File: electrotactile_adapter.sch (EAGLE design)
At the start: 15 parts, among them J3 PAD_SMD_L0.5_W1, J4 PAD_SMD_L0.5_W1, J5 PAD_SMD_L0.5_W1, J6 PAD_SMD_L0.5_W1, J7 1X33_MOLEX_FPC_FPC_RIBBON-CAB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, J8 1X33_MOLEX_FPC_FPC_RIBBON-CAB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

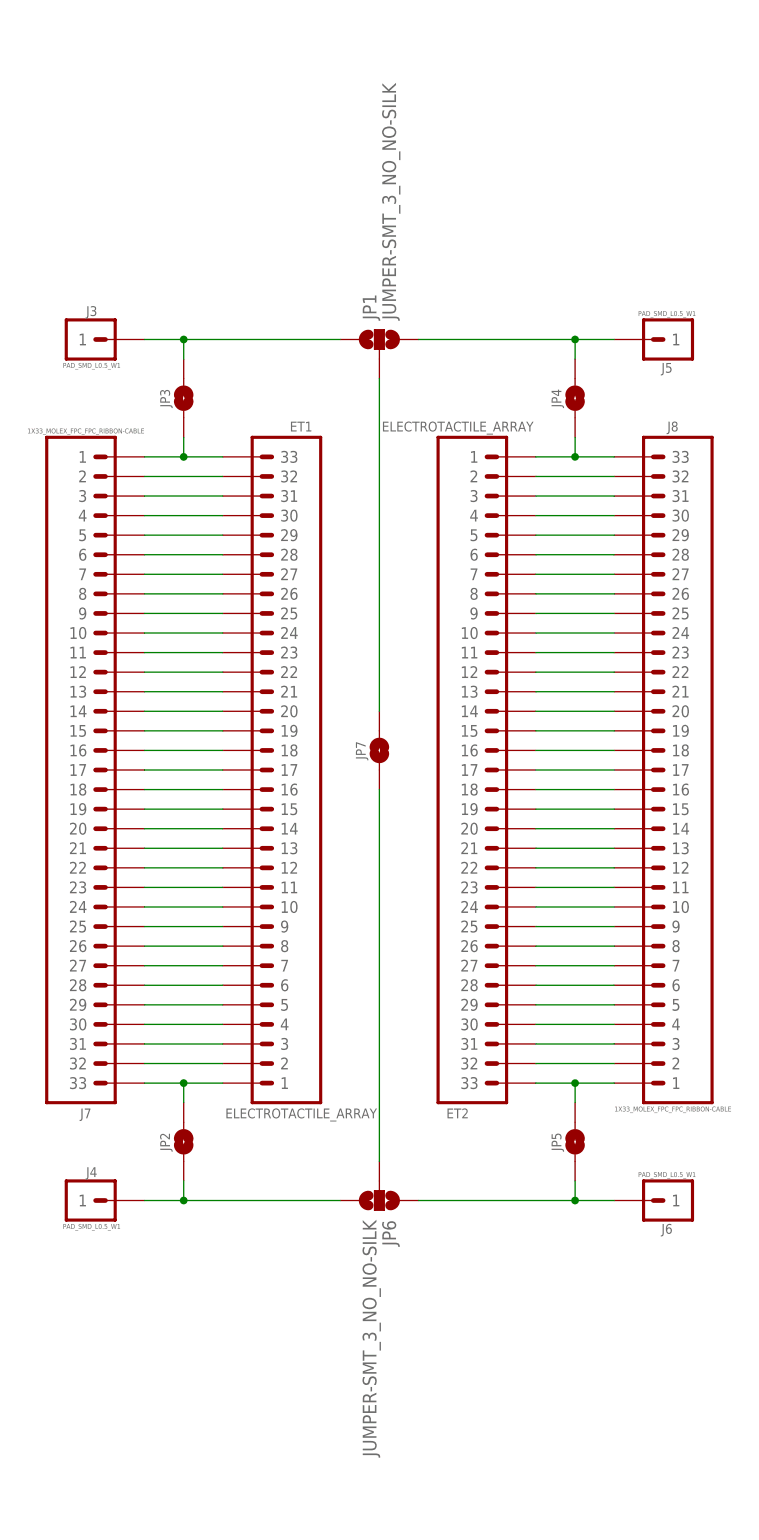
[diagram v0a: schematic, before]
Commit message: Update libraries with metadata.
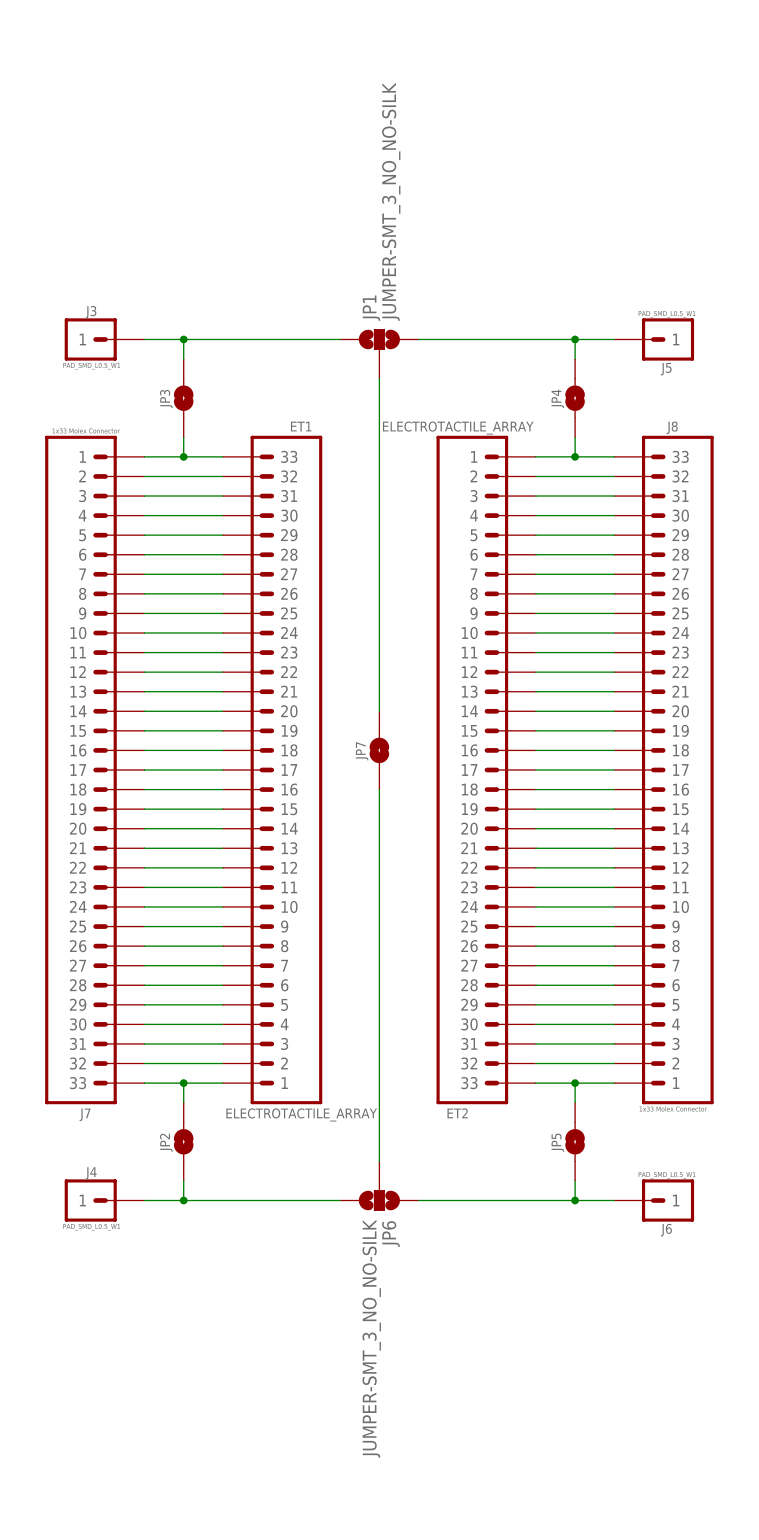
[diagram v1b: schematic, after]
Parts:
- J7, J8: value 1X33_MOLEX_FPC_FPC_RIBBON-CABLE -> 1x33 Molex Connector
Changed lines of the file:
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@@
 <part name="JP6" library="PiB_connectors" library_urn="urn:adsk.eagle:library:3661805" deviceset="JUMPER-SMT_3_NO" device="_NO-SILK" package3d_urn="urn:adsk.eagle:package:3661846/1"/>
 <part name="JP7" library="PiB_connectors" deviceset="JUMPER_SMD_2-PAD_NO" device="_SILK"/>
-<part name="J7" library="PiB_connectors" deviceset="1X33_MOLEX_FPC" device="_FPC_RIBBON-CABLE" package3d_urn="urn:adsk.eagle:package:3945547/2"/>
-<part name="J8" library="PiB_connectors" deviceset="1X33_MOLEX_FPC" device="_FPC_RIBBON-CABLE" package3d_urn="urn:adsk.eagle:package:3945547/2"/>
+<part name="J7" library="PiB_connectors" deviceset="1X33_MOLEX_FPC" device="_FPC_RIBBON-CABLE" package3d_urn="urn:adsk.eagle:package:3945547/2" value="1x33 Molex Connector"/>
+<part name="J8" library="PiB_connectors" deviceset="1X33_MOLEX_FPC" device="_FPC_RIBBON-CABLE" package3d_urn="urn:adsk.eagle:package:3945547/2" value="1x33 Molex Connector"/>
 </parts>
 <sheets>

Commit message: Rev 2.  Need to change size of ET cutout to 16mm x 12mm.
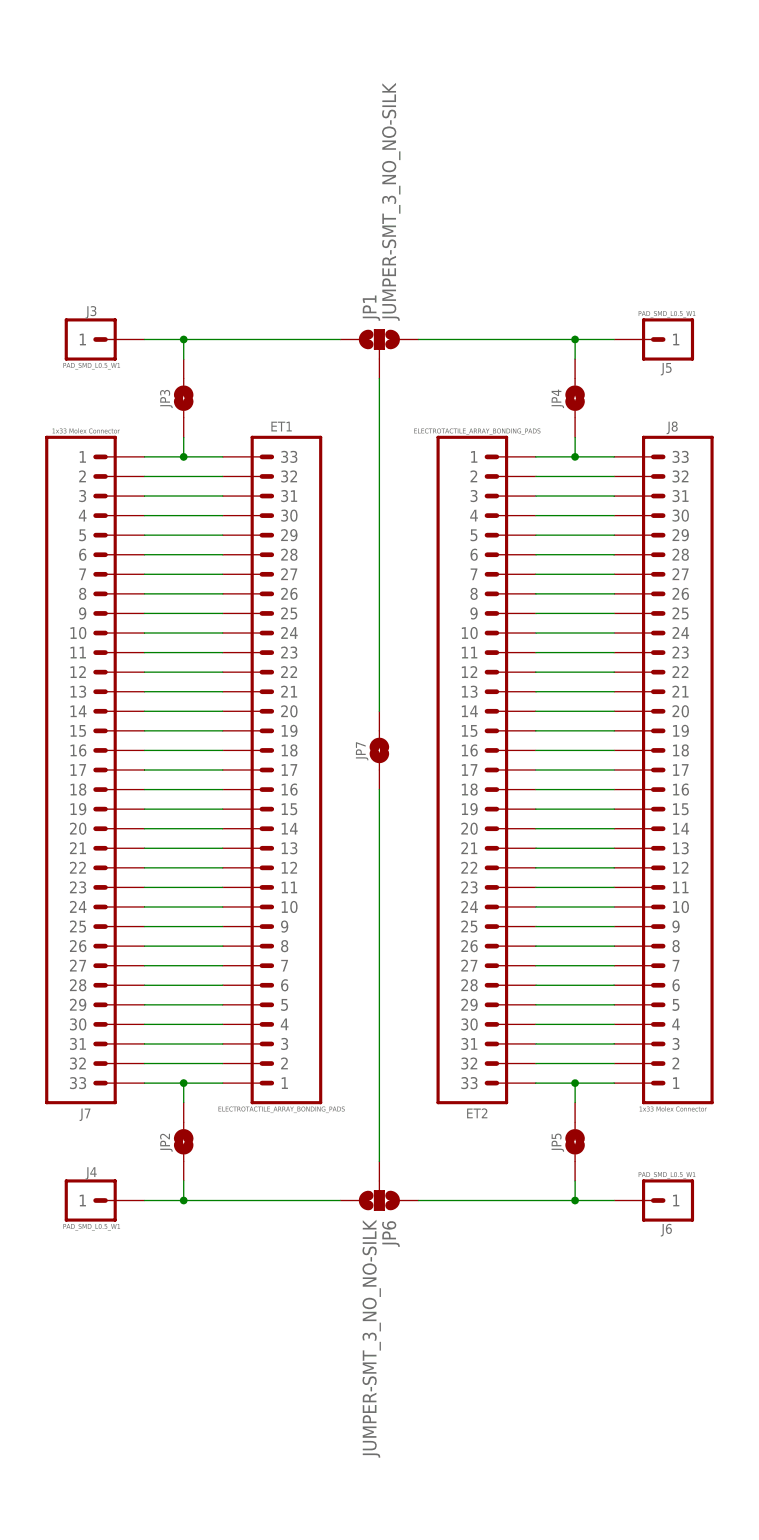
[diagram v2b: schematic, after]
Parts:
- added U$3: ELECTROTACTILE_SUBSTRATE, lipomi:ELECTROTACTILE_SUBSTRATE
- ET1, ET2: value ELECTROTACTILE_ARRAY -> ELECTROTACTILE_ARRAY_BONDING_PADS; device lipomi:ELECTROTACTILE_ARRAY -> lipomi:ELECTROTACTILE_ARRAY_BONDING_PADS
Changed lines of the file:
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@@
 <?xml version="1.0" encoding="utf-8"?>
 <!DOCTYPE eagle SYSTEM "eagle.dtd">
-<eagle version="9.1.0">
+<eagle version="9.1.3">
 <drawing>
 <settings>
@@
 </classes>
 <parts>
-<part name="ET2" library="lipomi" deviceset="ELECTROTACTILE_ARRAY" device=""/>
+<part name="ET2" library="lipomi" deviceset="ELECTROTACTILE_ARRAY_BONDING_PADS" device=""/>
 <part name="J6" library="PiB_connectors" deviceset="PAD_SMD" device="_L0.5_W1" value="PAD_SMD_L0.5_W1"/>
 <part name="J5" library="PiB_connectors" deviceset="PAD_SMD" device="_L0.5_W1" value="PAD_SMD_L0.5_W1"/>
-<part name="ET1" library="lipomi" deviceset="ELECTROTACTILE_ARRAY" device=""/>
+<part name="ET1" library="lipomi" deviceset="ELECTROTACTILE_ARRAY_BONDING_PADS" device=""/>
 <part name="JP1" library="PiB_connectors" library_urn="urn:adsk.eagle:library:3661805" deviceset="JUMPER-SMT_3_NO" device="_NO-SILK" package3d_urn="urn:adsk.eagle:package:3661846/1"/>
 <part name="J3" library="PiB_connectors" deviceset="PAD_SMD" device="_L0.5_W1" value="PAD_SMD_L0.5_W1"/>
@@
 <part name="J7" library="PiB_connectors" deviceset="1X33_MOLEX_FPC" device="_FPC_RIBBON-CABLE" package3d_urn="urn:adsk.eagle:package:3945547/2" value="1x33 Molex Connector"/>
 <part name="J8" library="PiB_connectors" deviceset="1X33_MOLEX_FPC" device="_FPC_RIBBON-CABLE" package3d_urn="urn:adsk.eagle:package:3945547/2" value="1x33 Molex Connector"/>
+<part name="U$3" library="lipomi" deviceset="ELECTROTACTILE_SUBSTRATE" device=""/>
 </parts>
 <sheets>
@@
 </plain>
 <instances>
-<instance part="ET2" gate="G$1" x="55.88" y="68.58" rot="MR180"/>
+<instance part="ET2" gate="G$1" x="58.42" y="68.58" rot="MR180"/>
 <instance part="J6" gate="G$1" x="83.82" y="10.16" rot="R180"/>
 <instance part="J5" gate="G$1" x="83.82" y="121.92" rot="R180"/>
-<instance part="ET1" gate="G$1" x="35.56" y="63.5" rot="MR0"/>
+<instance part="ET1" gate="G$1" x="33.02" y="63.5" rot="MR0"/>
 <instance part="JP1" gate="G$1" x="45.72" y="121.92" rot="R90"/>
 <instance part="J3" gate="G$1" x="7.62" y="121.92"/>

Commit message: update for Mickey.
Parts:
- removed U$3: ELECTROTACTILE_SUBSTRATE, lipomi:ELECTROTACTILE_SUBSTRATE
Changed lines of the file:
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@@
 <part name="J7" library="PiB_connectors" deviceset="1X33_MOLEX_FPC" device="_FPC_RIBBON-CABLE" package3d_urn="urn:adsk.eagle:package:3945547/2" value="1x33 Molex Connector"/>
 <part name="J8" library="PiB_connectors" deviceset="1X33_MOLEX_FPC" device="_FPC_RIBBON-CABLE" package3d_urn="urn:adsk.eagle:package:3945547/2" value="1x33 Molex Connector"/>
-<part name="U$3" library="lipomi" deviceset="ELECTROTACTILE_SUBSTRATE" device=""/>
 </parts>
 <sheets>
